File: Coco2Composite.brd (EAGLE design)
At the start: 64.7 x 39 mm, 21 parts, among them J1 TO_COCO2, J2 JACK_CONN1, J3 JACK_CONN2, J4 JACK_CONN3, J5 JACK_CONN4, J6 OUT_JACK, Q1 BC557, Q2 BC547, U1 MC1372

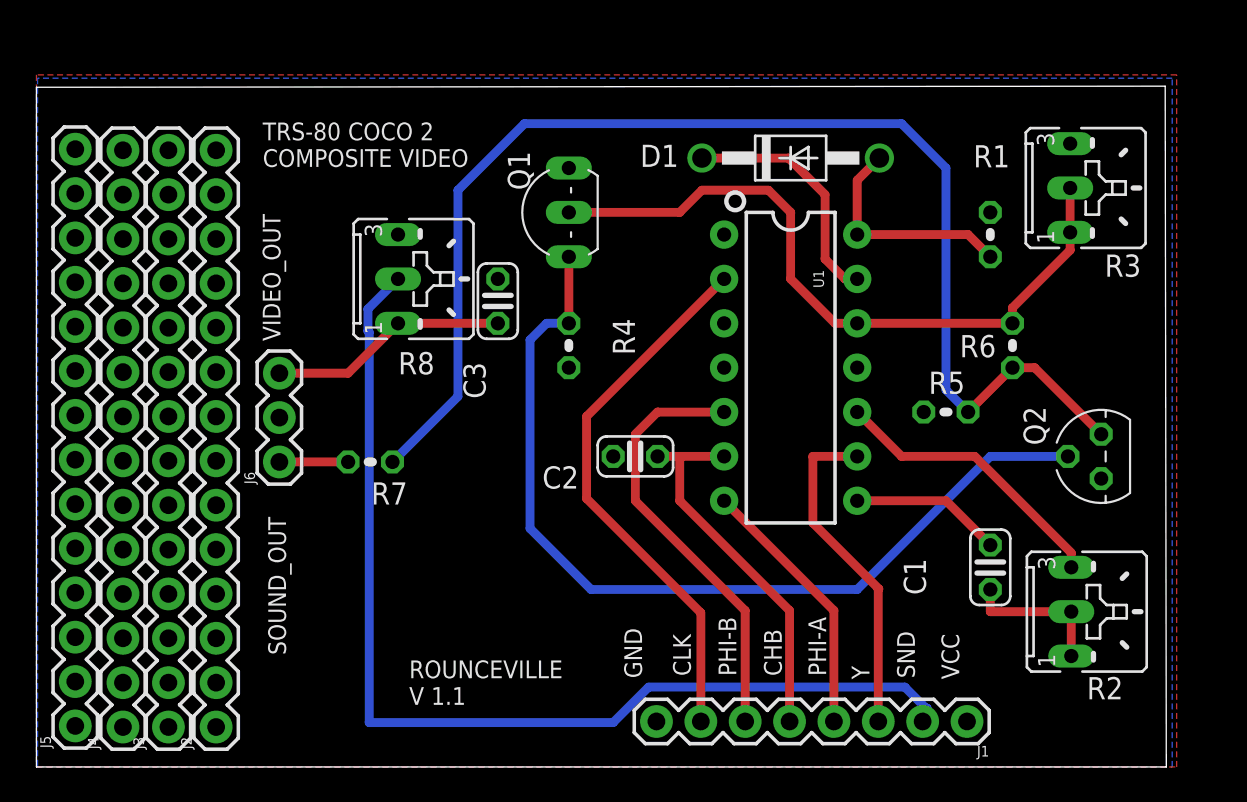
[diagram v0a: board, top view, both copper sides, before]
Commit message: Tried making a version for the horizontal RF mod
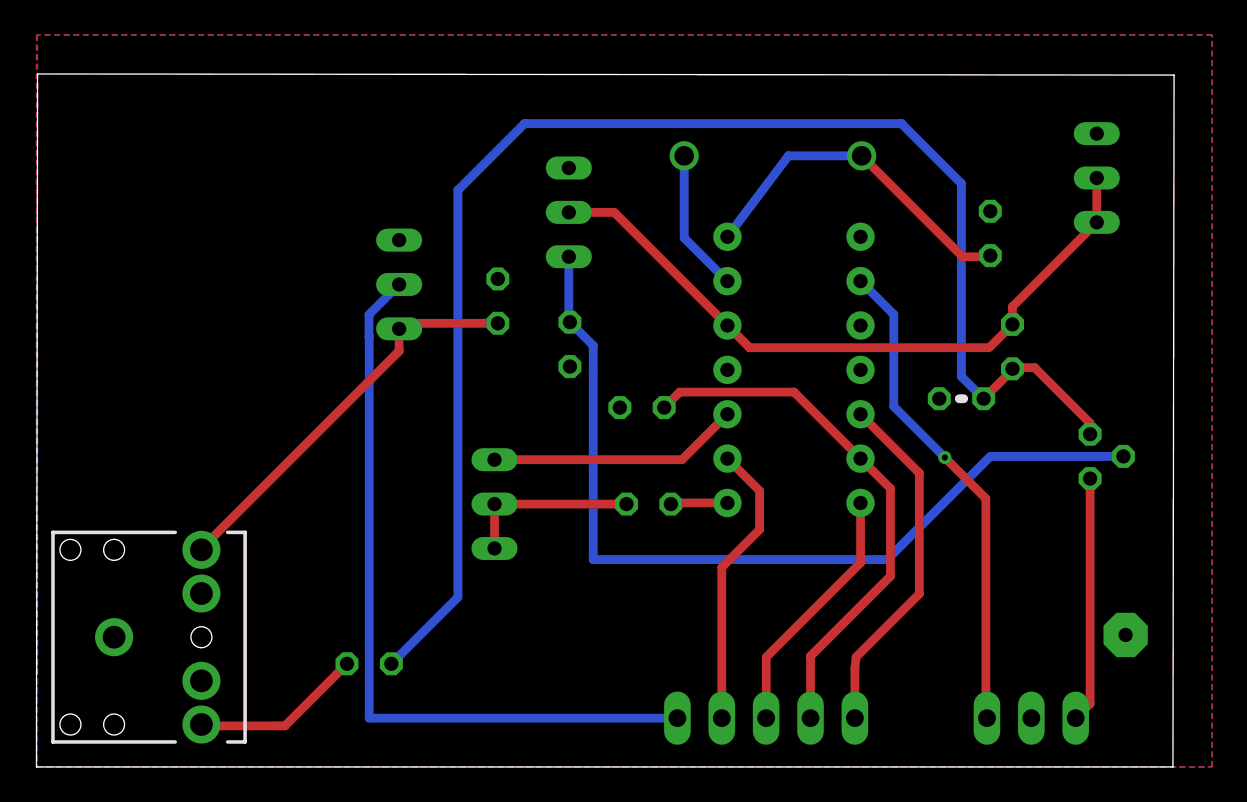
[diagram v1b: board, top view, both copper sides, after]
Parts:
- removed D1: 1N4004, diode:DO41-10
- removed J4: JACK_CONN3, SparkFun-Connectors:1X14
- removed J5: JACK_CONN4, SparkFun-Connectors:1X14
- removed J6: OUT_JACK, SparkFun-Connectors:1X03
- added D1-1N4001: 1N4004, diode:DO41-10
- added PAD1: (no value), wirepad:2,54/0,8
- J1: value TO_COCO2 -> (none); device SparkFun-Connectors:1X08 -> con-lstb:MA03-1
- J2: value JACK_CONN1 -> (none); device SparkFun-Connectors:1X14 -> con-lstb:MA05-1
- J3: value JACK_CONN2 -> AUDIO_JACK_3.5MM_PTH; device SparkFun-Connectors:1X14 -> SparkFun-Connectors:AUDIO-JACK
- moved R2 35.3 mm to (25.3, 15.0), flipped to the bottom
- moved J2 31.5 mm to (41.8, 2.79), flipped to the bottom, turned to 0 degrees
- moved C1 19.9 mm to (35.1, 15.0), flipped to the bottom, turned to 180 degrees
- moved R7 11.6 mm to (19.1, 5.91), flipped to the bottom, turned to 0 degrees
- moved J3 6.01 mm to (4.45, 7.43), turned to 0 degrees
- moved J1 3.69 mm to (57.0, 2.79), flipped to the bottom, turned to 0 degrees
- moved C2 2.82 mm to (34.7, 20.6), flipped to the bottom, turned to 0 degrees
- moved Q1 2.54 mm to (31.8, 31.8), flipped to the bottom
- moved R8 1.74 mm to (19.9, 27.6), flipped to the bottom
- moved R5 1.17 mm to (53.0, 21.1)
- moved Q2 0.63 mm to (60.3, 17.8), flipped to the bottom
- moved R3 0.63 mm to (59.8, 33.7), flipped to the bottom
- moved U1 0.23 mm to (43.4, 22.7), flipped to the bottom
- moved R4 0.09 mm to (30.5, 24.2), flipped to the bottom
- moved R1 0.06 mm to (54.6, 30.5), flipped to the bottom
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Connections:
- net CHB: now also J2.2; no longer J1.5
- net CLK: now also J1.3; no longer J1.7
- net GND: now also J3.SLEEVE, PAD1.1; no longer J1.8, J6.2
- net N$1: now also D1-1N4001.C; no longer D1.C
- net N$10: now also J3.RING; no longer J6.3
- net N$2: now also D1-1N4001.A; no longer D1.A
- net N$3: now also C1.2; no longer C1.1
- net N$4: now also C1.1; no longer C1.2
- net N$9: now also J3.TIP; no longer J6.1
- net PHIB: now also J2.1; no longer J1.6
- net PHI_A: now also J2.3; no longer J1.4
- net SND: now also J2.5; no longer J1.2
- net Y: now also J2.4; no longer J1.3
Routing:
- net SND: track 60.3 -> 43.2 mm
- net VCC: track 0.00 -> 14.1 mm
- net N$8: track 72.4 -> 82.3 mm
- net N$10: track 13.7 -> 23.0 mm
- net CHB: track 21.6 -> 30.6 mm
- net N$2: track 13.1 -> 19.8 mm
- net N$9: track 3.94 -> 9.79 mm
- net N$1: track 13.9 -> 8.20 mm
- net N$3: track 8.67 -> 3.24 mm
- net PHIB: track 24.7 -> 20.3 mm
- net CLK: track 31.3 -> 27.9 mm, vias 0 -> 1
- net Y: track 19.3 -> 16.5 mm
- net N$5: track 16.4 -> 14.4 mm
- net N$7: track 52.6 -> 50.7 mm
- net N$4: track 8.45 -> 10.1 mm
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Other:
- board size 64.7 x 39 mm -> 65.1 x 39.7 mm
- board text added: "ROUNCEVILLE V 1.0"
- board text removed: "ROUNCEVILLE V 1.1"
- board text removed: "SOUND_OUT"
- board text removed: "VIDEO_OUT"
